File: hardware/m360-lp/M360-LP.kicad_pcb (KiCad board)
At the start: 2 copper layers, 86 x 62 mm, 57 parts, among them J1 RJ45 SOLO, J2 RJ45 CLIMA/AUX, J3 J_VIN 3,0-6V, J4 M360-RF, Q1 AO3401A, Q2 AO3401A, SW1 Reed, U1 MCP1700T-3302E/TT, U2 74HC4051, U3 SRV05-4, U4 SRV05-4, U5 SRV05-4

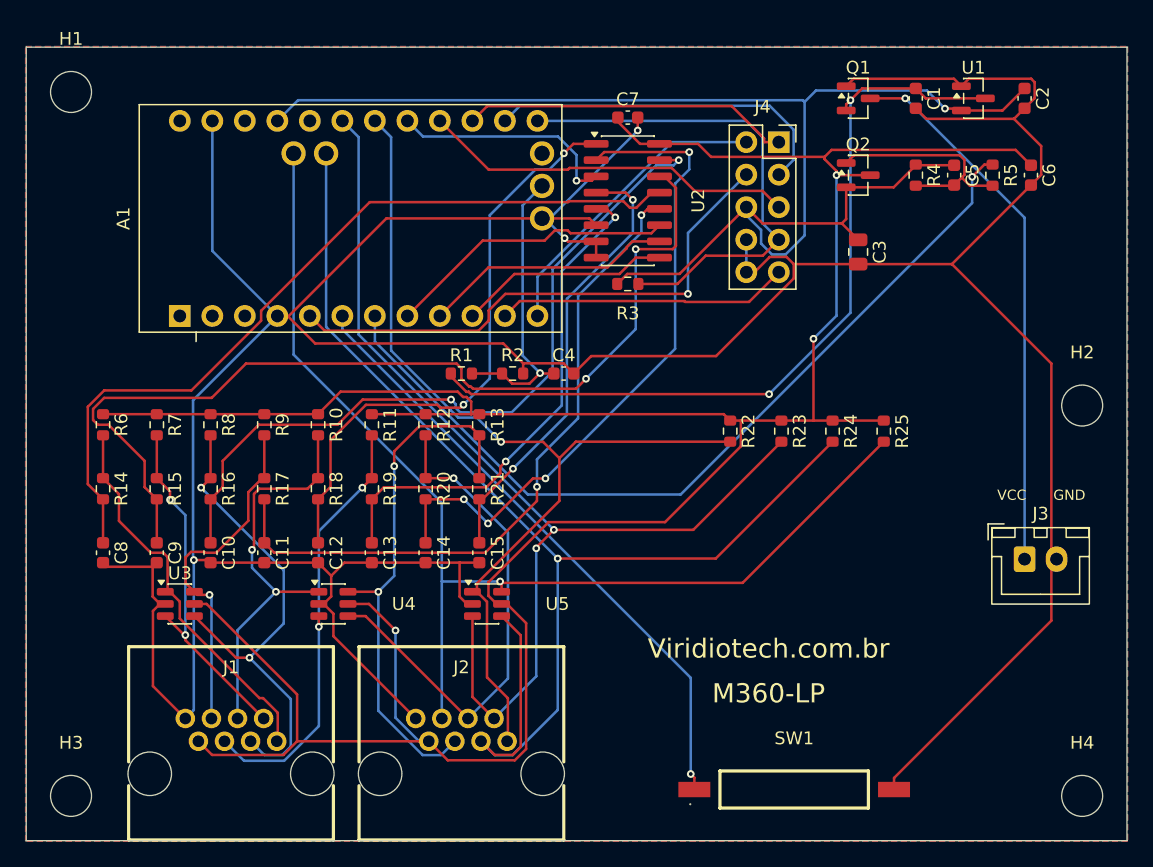
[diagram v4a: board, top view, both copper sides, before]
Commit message: feat(hardware): LP e ACT rerroteadas com o botão; GND volta a ser roteado
Conclui a troca do reed pelo botão iniciada em 0948368, que parou no esquemático.

Placas, para cada uma: del_fp.py SW1 → sincronização com o esquemático → place_*.py →
clear_tracks.py → export_dsn → dsn_sem_plano.py → Freerouting → import_ses →
zone_thermals.py → DRC com refill.

- M360-LP: 572 trilhas, 44 vias. DRC com 0 erros e 0 desconectados; restam os 8
  silk_edge_clearance dos RJ45, que já existiam.
- M360-ACT: 489 trilhas, 24 vias. DRC com 0 erros e 0 desconectados; restam os 13
  silk_edge_clearance, que já existiam. J1 em rot 0, como o place_act.py já pedia.
- Redes de todos os pads conferidas contra o HEAD: só o SW1 mudou. Trilhas todas de 0,25 mm.
- Paridade esquemático × placa com as mesmas contagens da base (237 e 195); some o
  footprint_symbol_mismatch do SW1.

**O GND não era roteado — e era isso que partia o plano.** Com zona de GND na placa, o DSN
declara `plane GND` e o Freerouting não desenha um fio de terra sequer. O primeiro roteamento
(bf701dc, 88 segmentos de GND) foi feito antes de as zonas existirem; todo rerroteamento
posterior perdia esse terra. Rerroteada com o DSN como sai do KiCad, a LP deu 16
unconnected_items, todos "Zona [GND]"; tirando as declarações plane, 0 — 100 segmentos de GND
na LP e 95 na ACT. Explica também os 15 desconectados imóveis da sessão anterior (§11.6).
Novo `tools/dsn_sem_plano.py`, e a §11 corrigida: 11.2, 11.4, 11.5 e 11.6.

Ajustes que o DRC pediu depois do rerroteamento:
- J4 da ACT, pino 8: starved_thermal → ligação sólida (pad_zone_connect.py), como o J3;
- silk_lp.py: referência do SW1 saía sobre "M360-LP"; vai para (172, 155);
- silk_act.py: referência do U1 encostava no J1, agora em rot 0; sobe para y = 143.

Botão: SHOU HAN TS665CJ, C393938, tátil 6 × 6 mm THT, SW1 nas três placas (LP, ACT e GW),
**solda manual e fora do PCBA**. Propriedade LCSC gravada nos três esquemáticos, com netlists
idênticas antes e depois. `add_lcsc.py` g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
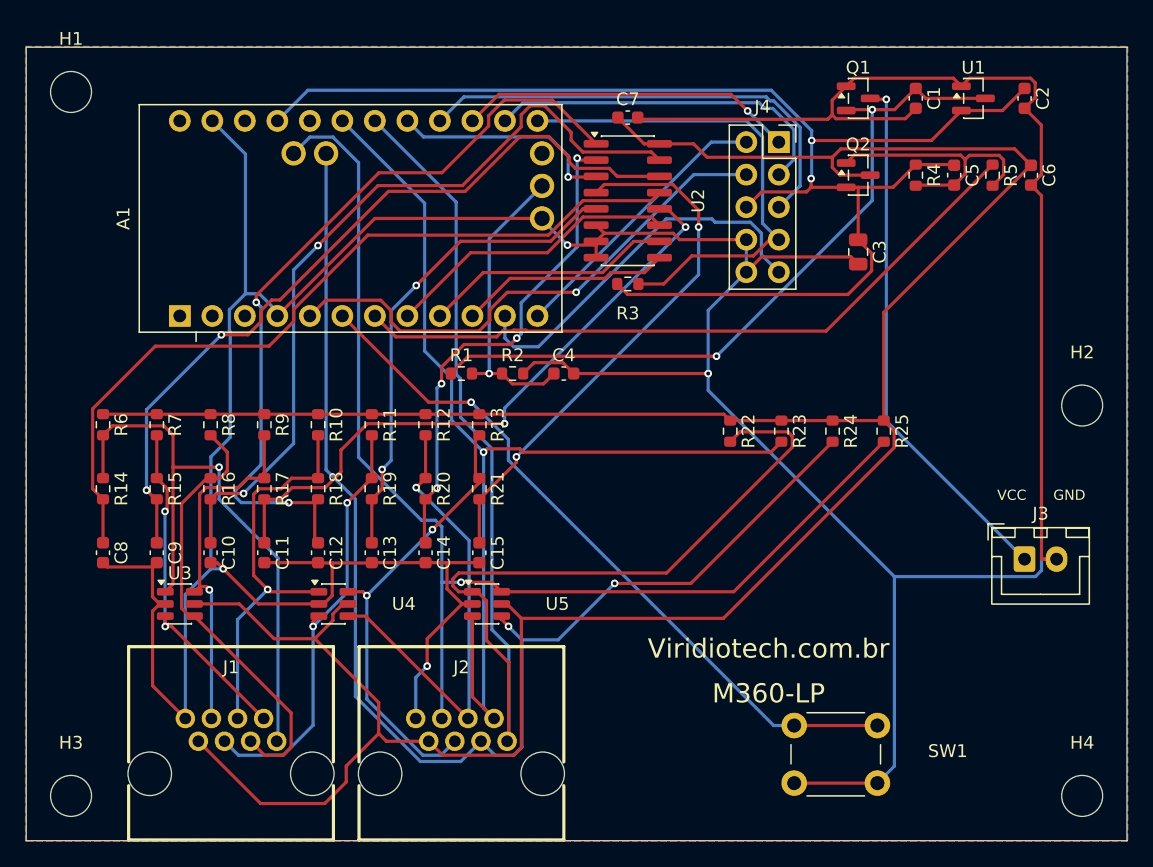
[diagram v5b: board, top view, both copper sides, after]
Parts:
- SW1: value Reed -> Repareamento; footprint M360:Reed_Littelfuse_59170 -> Button_Switch_THT:SW_PUSH_6mm
- moved SW1 5.00 mm to (160.0, 153.0)
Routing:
- net ONEWIRE: track 75.1 -> 105.2 mm, vias 1 -> 0
- net GND: track 315.2 -> 337.1 mm, vias 3 -> 4
- net SOIL0: track 30.6 -> 48.9 mm, vias 0 -> 1
- net SOIL4_F: track 46.5 -> 61.5 mm
- net SOIL1_F: track 75.8 -> 61.7 mm
- net SOIL6_F: track 52.7 -> 38.7 mm
- net VSW_EN: track 67.1 -> 54.6 mm, vias 1 -> 0
- net REED: track 48.4 -> 56.0 mm
- net SCK: track 29.4 -> 36.8 mm
- net RF_RESET: track 22.9 -> 30.3 mm
- net SOIL7_F: track 35.0 -> 42.2 mm
- net SOIL7: track 42.1 -> 35.3 mm
- net VIN: track 63.4 -> 57.5 mm
- net SOIL2: track 39.2 -> 34.6 mm, vias 2 -> 0
- net SOIL3_F: track 54.0 -> 49.5 mm
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
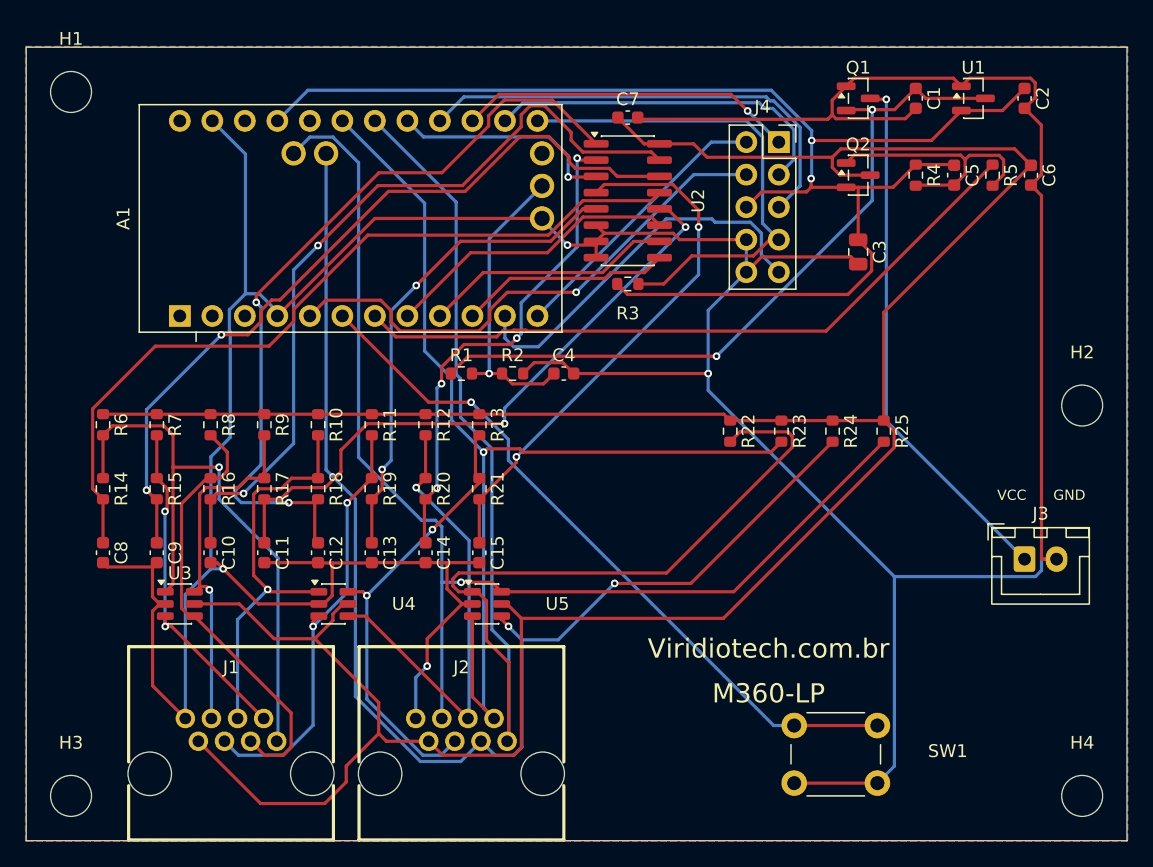
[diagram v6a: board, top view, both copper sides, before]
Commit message: feat(hardware): placa da M360-LP refeita sobre o esquemático corrigido
Sequência da §11.5: del_fp.py SW1 (botão → reed) → sincronização → place_lp.py →
clear_tracks.py → export_dsn (conferido: 61 peças, R25/R29 presentes, sem U8/J5, width 250,
0 fios) → dsn_sem_plano.py → Freerouting → import_ses → zone_thermals.py → silk_lp.py → DRC com
refill → pad_zone_connect.py J1 8 → solda_manual.py.

- Reed de volta em (160, 158); R26–R29 (100 Ω em série das digitais) numa fileira em y = 136,
  entre o TVS U5 e os pull-ups, mesmo passo e orientação destes. Sem sobreposição de courtyard.
- 606 trilhas de 0,25 mm e 47 vias; GND roteado (plano retirado do DSN).
- **DRC `--severity-all`: 0 violações e 0 pendências**, como pede o fluxo de hardware do
  projeto. Isso inclui os 8 `silk_edge_clearance` dos RJ45 que a placa carregava: eram a linha
  frontal, o fim das laterais e um círculo de 0,03 mm da serigrafia do footprint, colados na
  borda. Novo `tools/fix_rj45_silk.py` corrige a biblioteca e as cópias em todas as placas (a ACT
  recebe só esses 12 traços; continua defasada).
- `paridade.py`: idêntica ao esquemático. Arquivo de posição sem A1, J1–J4.
- Serigrafia: legenda "FTDI sem VCC" na faixa entre a borda e o Pro Mini; marca do pino 1 do
  soquete do mezanino; referência do U3 tirada de cima do "C9" (visto só no render 3D).

Documentação: status, §9 (placas defasadas: falta ACT e GW), §10, §11.4 e README das
ferramentas.

Co-Authored-By: Claude Opus 5 (1M context) <noreply@anthropic.com>
Claude-Session: https://claude.ai/code/session_012t7RkcrXvvpDVjKVimNu18
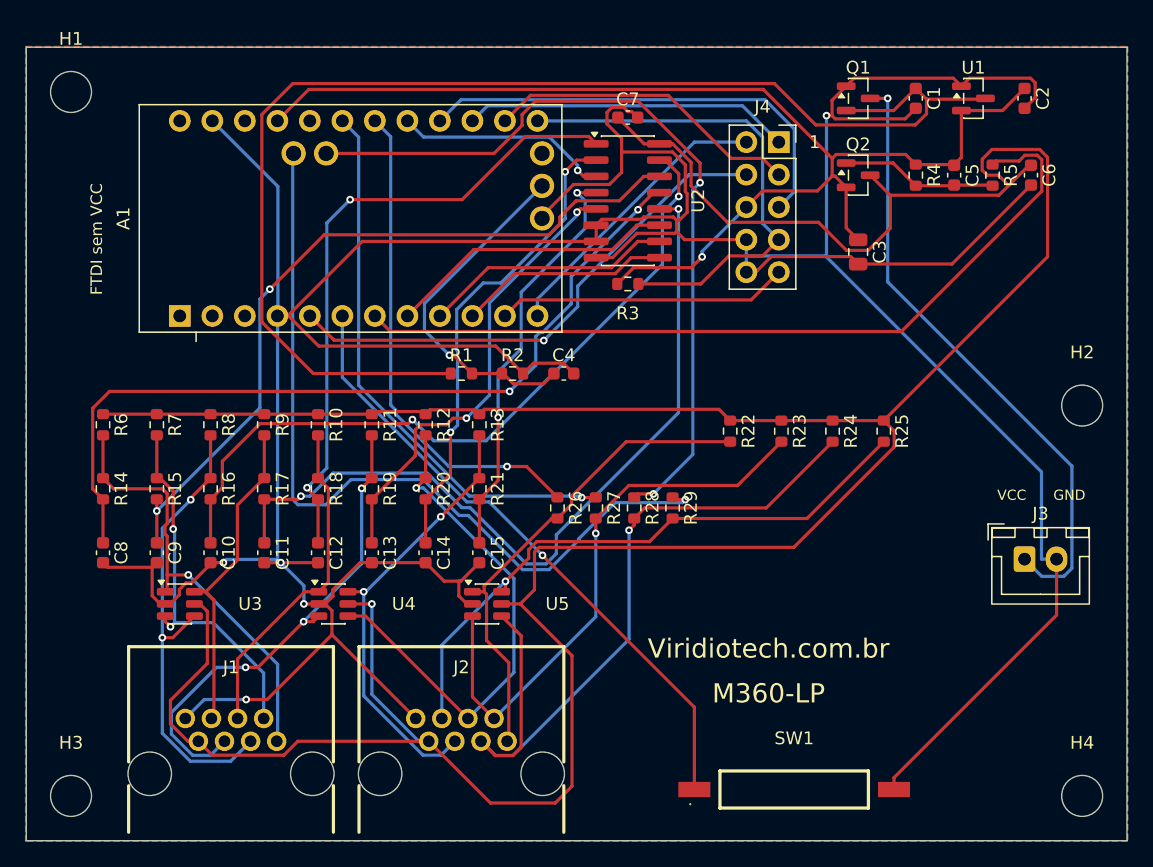
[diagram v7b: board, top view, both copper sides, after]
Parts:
- added R26: 100, Resistor_SMD:R_0603_1608Metric, F.Cu at (141.5, 136.0)
- added R27: 100, Resistor_SMD:R_0603_1608Metric, F.Cu at (144.5, 136.0)
- added R28: 100, Resistor_SMD:R_0603_1608Metric, F.Cu at (147.5, 136.0)
- added R29: 100, Resistor_SMD:R_0603_1608Metric, F.Cu at (150.5, 136.0)
- SW1: value Repareamento -> Reed; footprint Button_Switch_THT:SW_PUSH_6mm -> M360:Reed_Littelfuse_59170
- moved SW1 5.00 mm to (160.0, 158.0)
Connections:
- A1 pad 18: ONEWIRE -> ONEWIRE_MCU
- A1 pad 19: DHT -> DHT_MCU
- A1 pad 25: SDA -> SDA_MCU
- A1 pad 26: SCL -> SCL_MCU
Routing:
- net ONEWIRE: track 105.2 -> 38.2 mm
- net SCL_MCU: track 0.00 -> 65.0 mm, vias 0 -> 1
- net SDA_MCU: track 0.00 -> 62.4 mm, vias 0 -> 2
- net SCL: track 92.9 -> 48.2 mm
- net DHT_MCU: track 0.00 -> 43.4 mm, vias 0 -> 1
- net SDA: track 101.4 -> 58.1 mm, vias 2 -> 1
- net VIN: track 57.5 -> 100.4 mm, vias 2 -> 0
- net DHT: track 84.1 -> 44.6 mm
- net ONEWIRE_MCU: track 0.00 -> 38.9 mm, vias 0 -> 1
- net VSW: track 228.7 -> 258.4 mm, vias 0 -> 1
- net 3V3: track 112.4 -> 94.6 mm, vias 2 -> 1
- net SOIL0: track 48.9 -> 34.3 mm
- net SOIL3_F: track 49.5 -> 62.7 mm
- net SOIL4_F: track 61.5 -> 50.1 mm
- net SOIL7_F: track 42.2 -> 32.5 mm
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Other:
- board text added: "1"
- board text added: "FTDI sem VCC"

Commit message: fix(hardware): M360-LP — correções da revisão adversarial de placa
- TVS como primeiro pad nas 13 linhas de campo, provado por ordem_tvs.py:
  leque fixo dos TVS (leque_tvs.py), pernas RJ45 -> TVS roteadas antes e
  cobertas por área proibida (dsn_trechos.py), U3/U5 a 180°, R26-R29 acima do U5
- reed na borda esquerda; VIN/VIN_RAW/3V3 em 0,5 mm (classe Power); C3 junto do U1
- GND: 48 vias (eram 5), vias no J1.8/J2.8, costura do perímetro (vias_gnd.py);
  área sem trilha em B.Cu sob os RJ45 a partir de y 150,6
- fiduciais, legendas de 1,0 mm, apara_pontas.py para tocos soltos
- datasheets do reed, RJ45 e JST em docs/datasheets com índice
- ARQUITETURA §11.8 (fluxo e limite de projeto: canais dos TVS fora da ordem
  dos pinos do RJ45) e §9 (distância do ímã, achados 7 e 8 aceitos)

DRC --severity-all: 0 violações, 0 pendências; paridade.py idêntica.

Co-Authored-By: Claude Opus 5 (1M context) <noreply@anthropic.com>
Claude-Session: https://claude.ai/code/session_012t7RkcrXvvpDVjKVimNu18
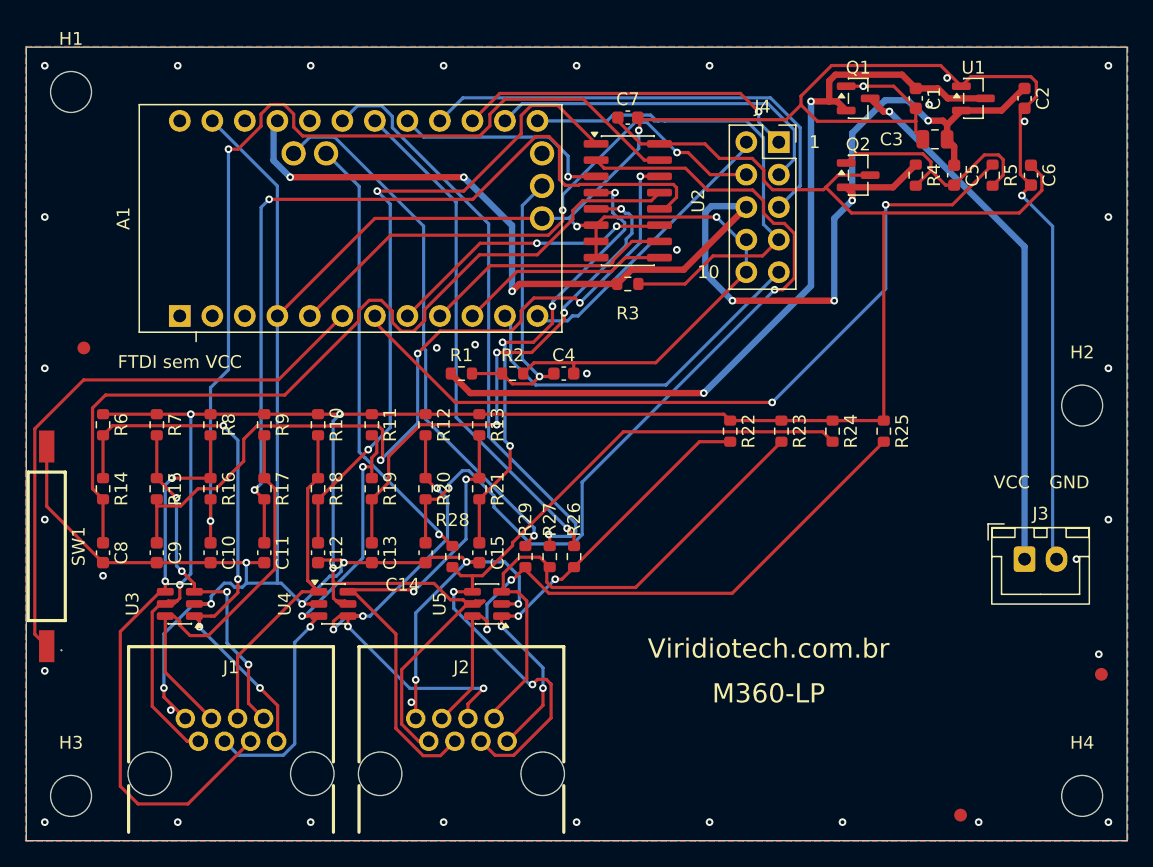
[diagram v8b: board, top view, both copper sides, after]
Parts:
- added FID1: Fiducial_1mm_Mask2mm, Fiducial_1mm_Mask2mm, F.Cu at (104.5, 123.5)
- added FID2: Fiducial_1mm_Mask2mm, Fiducial_1mm_Mask2mm, F.Cu at (184.0, 149.0)
- added FID3: Fiducial_1mm_Mask2mm, Fiducial_1mm_Mask2mm, F.Cu at (173.0, 160.0)
- moved SW1 61.4 mm to (101.6, 139.0), turned to 90 degrees
- moved R28 14.7 mm to (133.3, 139.8)
- moved R29 12.1 mm to (139.0, 139.8)
- moved C3 10.7 mm to (171.0, 107.2), turned to 180 degrees
- moved R27 5.23 mm to (140.9, 139.8)
- moved R26 4.02 mm to (142.8, 139.8)
- turned U3 to 180 degrees
- turned U5 to 180 degrees
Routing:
- net VSW: track 258.4 -> 194.4 mm, vias 1 -> 4
- net GND: track 337.1 -> 297.0 mm, vias 5 -> 48
- net VIN: track 100.4 -> 64.5 mm, vias 0 -> 2
- net SOIL6_F: track 37.2 -> 69.1 mm
- net SDA_MCU: track 62.4 -> 34.9 mm, vias 2 -> 1
- net SCL_MCU: track 65.0 -> 42.4 mm
- net 3V3: track 94.6 -> 110.3 mm, vias 1 -> 7
- net SOIL2_F: track 58.4 -> 74.0 mm
- net SOIL2: track 36.5 -> 45.1 mm
- net SOIL0: track 34.3 -> 42.6 mm, vias 1 -> 4
- net VIN_RAW: track 48.6 -> 41.3 mm
- net VSW_G: track 12.2 -> 19.2 mm
- net SOIL3: track 25.3 -> 31.8 mm
- net SOIL1_F: track 58.8 -> 65.2 mm, vias 2 -> 4
- net RF_RESET: track 22.8 -> 29.0 mm
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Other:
- board text added: "10"
